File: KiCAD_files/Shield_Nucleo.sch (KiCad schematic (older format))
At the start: 125 parts, among them J1 Conn_01x02, J2 RJ45_LED_Shielded, J3 RJ45_LED_Shielded, J4 Conn_01x03_Male, J5 Conn_01x05_Male, J6 Conn_01x02, J7 Power, J8 Conn_02x07_Odd_Even, SW1 SW_Push, U1 STM32G474RE, U2 AT25xxx, U3 TCAN334GDR, U4 AP1117-33, U5 UCC21222DR, U6 UCC21222DR, U7 SFH617A-2X009T, U8 RFM-0505s, U9 RFM-0505s, Y1 ECS-240-10-33-AGM-TR - 24MHz

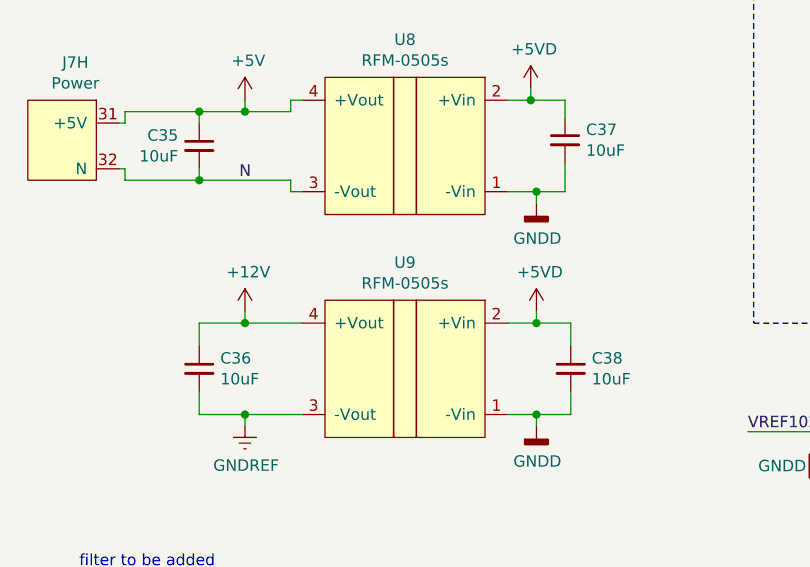
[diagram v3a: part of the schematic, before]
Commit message: Correct reference U9 ShieldNucleo
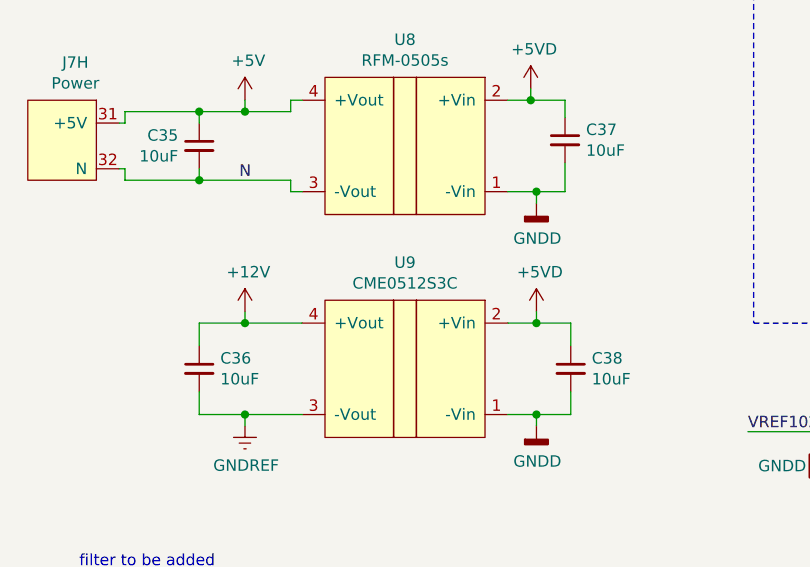
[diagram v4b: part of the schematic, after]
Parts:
- U9: value RFM-0505s -> CME0512S3C; Manf# ROE0505S -> CME0512S3C
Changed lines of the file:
@@
 P 14600 9350
 F 0 "U9" H 14600 9815 50  0000 C CNN
-F 1 "RFM-0505s" H 14600 9724 50  0000 C CNN
+F 1 "CME0512S3C" H 14600 9724 50  0000 C CNN
 F 2 "Converter_DCDC:Converter_DCDC_muRata_CRE1xxxxxx3C_THT" H 14600 9700 50  0001 C CNN
-F 3 "https://recom-power.com/pdf/Econoline/ROE.pdf" H 14600 9700 50  0001 C CNN
-F 4 "ROE0505S" H 14600 9350 50  0001 C CNN "Manf#"
+F 3 "https://www.murata.com/products/productdata/8807029342238/kdc-cme.pdf?1614569448000" H 14600 9700 50  0001 C CNN
+F 4 "CME0512S3C" H 14600 9350 50  0001 C CNN "Manf#"
 	1    14600 9350
 	-1   0    0    -1

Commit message: Add ShieldNucleo Bom, Power Bom and Kicost Price for both
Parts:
- PS4, PS5: MANUFACTURER CUI Inc. -> (none)
- U1: Manf# STM32G474RE -> STM32G474RET6
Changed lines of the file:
@@
 F 2 "Package_QFP:LQFP-64_10x10mm_P0.5mm" H 3100 2075 50  0001 R CNN
 F 3 "https://my2.st.com/resource/en/datasheet/stm32g474re.pdf" H 3700 3775 50  0001 C CNN
-F 4 "STM32G474RE" H 3700 3775 50  0001 C CNN "Manf#"
+F 4 "STM32G474RET6" H 3700 3775 50  0001 C CNN "Manf#"
 	1    3700 3775
 	1    0    0    -1
@@
 F 2 "Footprints:PQDE6W-Q110-S5-D" H 20800 7325 50  0001 L BNN
 F 3 "https://www.cui.com/product/resource/pqde6w-q110-d.pdf" H 20250 7825 50  0001 L BNN
-F 4 "CUI Inc." H 20250 7825 50  0001 L BNN "MANUFACTURER"
+F 4 "" H 20250 7825 50  0001 L BNN "MANUFACTURER"
 F 5 "3.5 mm" H 20250 7825 50  0001 L BNN "MAXIMUM_PACKAGE_HEIGHT"
 F 6 "Manufacturer Recommendations" H 20800 7325 50  0001 L BNN "STANDARD"
@@
 F 2 "Footprints:CONV_VXO78012-500-M" H 20800 8125 50  0001 L BNN
 F 3 "https://www.cui.com/product/resource/vxo78-500-m.pdf" H 20250 8625 50  0001 L BNN
-F 4 "CUI Inc." H 20250 8625 50  0001 L BNN "MANUFACTURER"
+F 4 "" H 20250 8625 50  0001 L BNN "MANUFACTURER"
 F 5 "3.5 mm" H 20250 8625 50  0001 L BNN "MAXIMUM_PACKAGE_HEIGHT"
 F 6 "Manufacturer Recommendations" H 20800 8125 50  0001 L BNN "STANDARD"

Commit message: WIP : Closed all issues rised with V1.1.1 prototype.
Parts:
- removed JP4: SolderJumper_2_Open, Jumper:SolderJumper-2_P1.3mm_Open_Pad1.0x1.5mm, symbol Jumper:SolderJumper_2_Open
- removed R26, R27: 100K, Resistor_SMD:R_0805_2012Metric, symbol Device:R_Small
- added C41, C43, C44: 1µF, Capacitor_SMD:C_0805_2012Metric, symbol Device:C_Small
- added C42: 100nF, Capacitor_SMD:C_0805_2012Metric, symbol Device:C_Small
- added unit 9 of J7
- added J9: Conn_01x03, Connector_PinHeader_2.54mm:PinHeader_1x03_P2.54mm_Vertical, symbol Connector_Generic:Conn_01x03
- added JP4: Jumper, Connector_PinHeader_2.54mm:PinHeader_1x02_P2.54mm_Vertical, symbol Device:Jumper
- added LED2: PWR, LED_SMD:LED_0805_2012Metric, symbol Device:LED
- added R26: 330, Resistor_SMD:R_0805_2012Metric, symbol Device:R
- added U10: MCP1799T-5002H/TT, Package_TO_SOT_SMD:SOT-23, symbol Regulator_Linear:MCP1754S-5002xCB
- R2, R3, R4, R5, R6, R7, R8: value 20k -> 100
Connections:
- net +12V: now also C44.1, U10.3 (VI)
- net +3V3: now also LED2.2 (A)
- net +5VD: now also J9.1 (Pin_1), JP4.1; no longer C19.1, PS4.4 (+VO), PS5.3 (+VO)
- net GNDD: now also C41.2, C42.2, J9.3 (Pin_3), R26.2
- net GNDREF: now also C43.2, C44.2, U10.1 (GND)
- net VREF2048: now also C41.1, C42.1
- new net: LED2.1 (K), R26.1
- new net +5P: C43.1, J7.33 (+5VP), U10.2 (VO)
- new net +5VJP: C19.1, JP4.2, PS4.4 (+VO), PS5.3 (+VO)
- no-connect marks 9 -> 10
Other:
- note added: "1.024V VREF signal come from SoC integrated DAC2.\n"
- note removed: "Two ways of having a 1.024V VREF signal\n- a stupid hardware based one \n- a DAC based solutions that needs to \nwork on the software side\n"
- note removed: "filter to be added\n"
- moved on the sheet: C35, C36, C37, C38, J4, J5, J7F, J7H, J8, JP3, LED1, R24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

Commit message: Added gerbers files used for PCB order
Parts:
- removed J4: Conn_01x03_Male, Connector_PinHeader_2.54mm:PinHeader_1x03_P2.54mm_Vertical, symbol Connector:Conn_01x03_Male
- removed J5: Conn_01x05_Male, Connector_PinHeader_2.54mm:PinHeader_1x05_P2.54mm_Vertical, symbol Connector:Conn_01x05_Male
- added J4, J5: Conn_01x06_Male, Connector_PinHeader_2.54mm:PinHeader_1x06_P2.54mm_Vertical, symbol Connector:Conn_01x06_Male
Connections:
- net +3V3: now also J4.1 (Pin_1), J5.2 (Pin_2)
- net +5VD: now also J4.6 (Pin_6)
- net GNDD: now also J4.5 (Pin_5), J5.1 (Pin_1)
- net SPI3_CS2: now also J5.6 (Pin_6)
- net SPI3_MISO: now also J5.3 (Pin_3)
- net SPI3_MOSI: now also J5.4 (Pin_4)
- net SPI3_SCK: now also J5.5 (Pin_5)
- net USART1_RX: now also J4.3 (Pin_3)
- net USART1_TX: now also J4.4 (Pin_4)
- new net DTR: J4.2 (Pin_2)
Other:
- note added: "Standard headers for SPI and UART modules"
- moved on the sheet: C19, C29, C39, C40, J7D, J7F, J8, J9, JP4, LED1, LED2, PS4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
